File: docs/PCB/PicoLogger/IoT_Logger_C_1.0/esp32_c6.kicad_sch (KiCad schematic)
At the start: 23 parts, among them J2 ESP_UART, Q1 BSS138, Q2 AO3407, SW1 Tact Switch 6x6mm / 13mm, SW2 Tact Switch 6x6mm / 13mm, U2 ESP32-C6-WROOM-1U

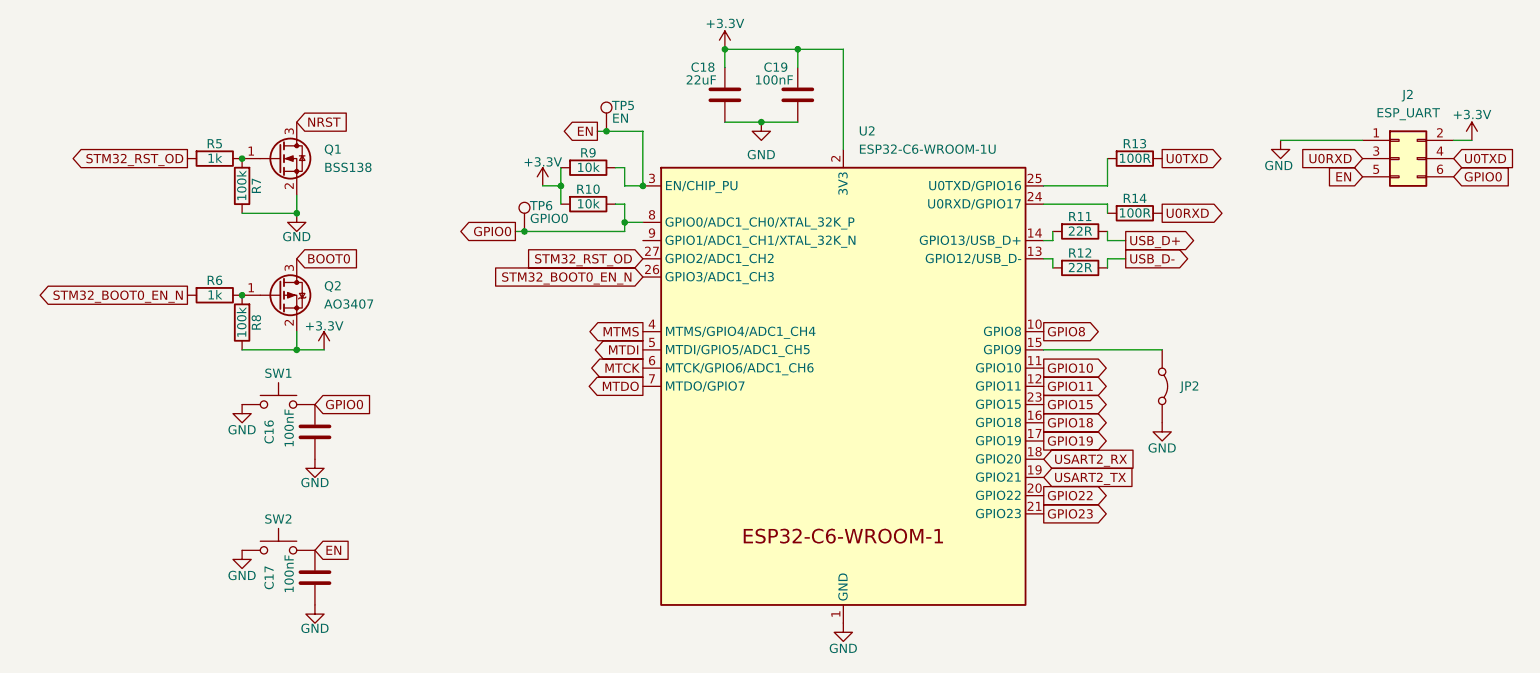
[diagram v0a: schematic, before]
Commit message: Logger IoT B and C production files generated, backend and frontend prepared for new logger type.
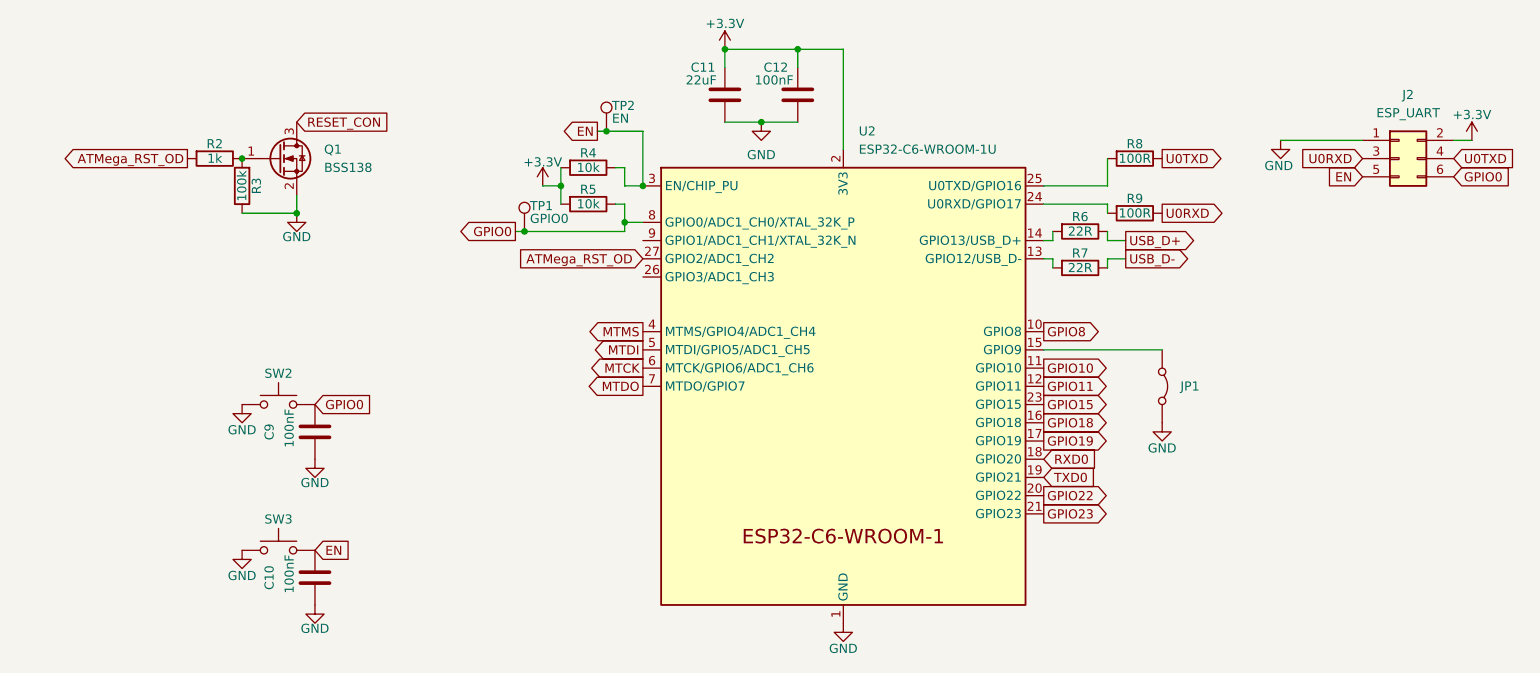
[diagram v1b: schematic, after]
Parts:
- removed Q2: AO3407, Package_TO_SOT_SMD:SOT-23, symbol Transistor_FET:AO3401A
- removed R6: 1k, Resistor_SMD:R_0603_1608Metric, symbol Device:R
- removed R8: 100k, Resistor_SMD:R_0603_1608Metric, symbol Device:R
- J2: footprint Connector_IDC:IDC-Header_2x03_P2.54mm_Vertical -> Connector_PinHeader_1.27mm:PinHeader_2x03_P1.27mm_Vertical
- renumbered C17 to C10, C18 to C11, C19 to C12, C16 to C9, JP2 to JP1, R5 to R2, R7 to R3, R9 to R4, R10 to R5, R11 to R6, R12 to R7, R13 to R8, R14 to R9, SW1 to SW2, SW2 to SW3, TP6 to TP1, TP5 to TP2
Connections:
- net NRST renamed RESET_CON
- net STM32_BOOT0_EN_N: no longer names the net of U2.26 (GPIO3/ADC1_CH3)
- net STM32_RST_OD renamed ATMega_RST_OD
- net USART2_RX renamed RXD0
- net USART2_TX renamed TXD0
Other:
- title: IoT Logger A - ESP32 C6 -> IoT Logger C - ESP32 C6

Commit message: Code added, documentation review.
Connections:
- net GPIO1: now reaches U2.9 (GPIO1/ADC1_CH1/XTAL_32K_N)
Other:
- moved on the sheet: R4, R5, TP1, TP2

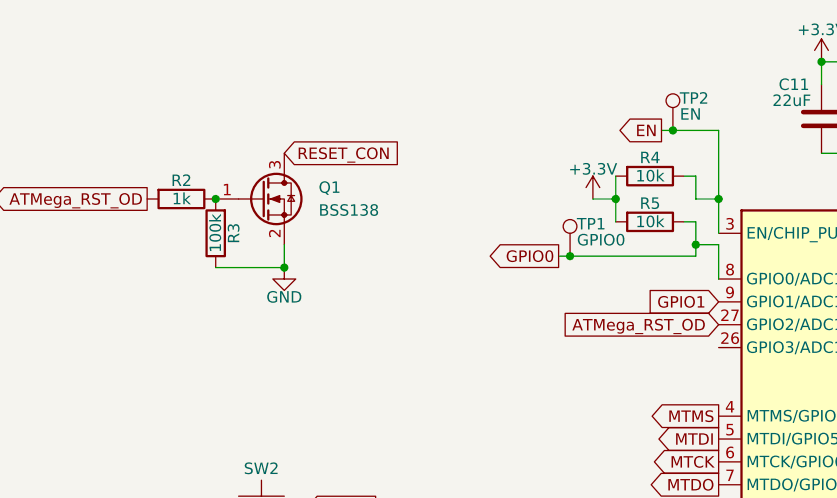
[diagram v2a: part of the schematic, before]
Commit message: New logger revisions added.
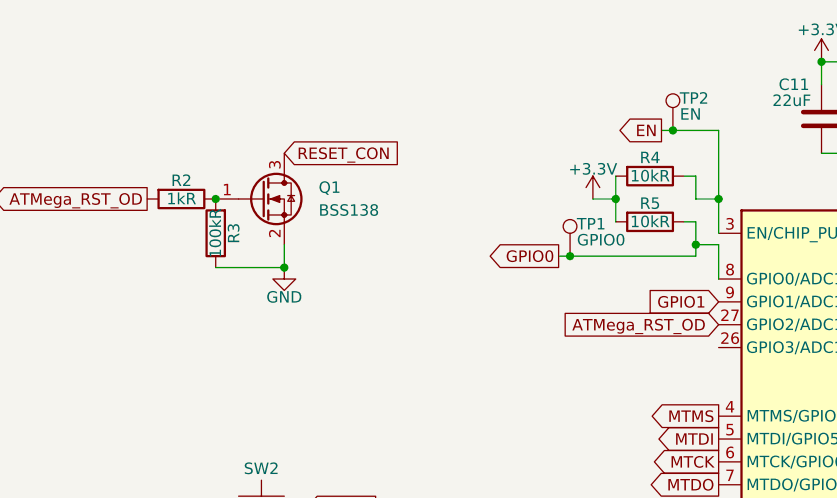
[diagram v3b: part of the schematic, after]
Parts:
- R2: value 1k -> 1kR
- R3: value 100k -> 100kR
- R4, R5: value 10k -> 10kR
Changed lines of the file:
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@@
 			)
 		)
-		(property "Value" "1k"
+		(property "Value" "1kR"
 			(at 68.58 69.85 90)
 			(effects
@@
 			)
 		)
-		(property "Value" "100k"
+		(property "Value" "100kR"
 			(at 72.39 73.66 90)
 			(effects
@@
 			)
 		)
-		(property "Value" "10k"
+		(property "Value" "10kR"
 			(at 120.65 67.31 90)
 			(effects
@@
 			)
 		)
-		(property "Value" "10k"
+		(property "Value" "10kR"
 			(at 120.65 72.39 90)
 			(effects
